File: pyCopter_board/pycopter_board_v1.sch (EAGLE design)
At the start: 53 parts, among them IC1 STM32F405RGT, Q1 8MHz, Q2 32.768kHz, U1 MCP1802

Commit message: Added BNO055 chip library. Also started pyCopter board V1 in board folder. BNO055 connections are almost finished, just need to finish I2C connections.
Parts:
- removed C10, C16, C17: 1u, rcl:C-EUC0603
- removed C11, C12: 12p, rcl:C-EUC0603
- removed C11B, C12B: 2u2, rcl:C-EUC0603
- removed C13, C6, C8, C9: 100n, rcl:C-EUC0603
- removed C7: 4u7, rcl:C-EUC0603
- removed D1: 1N5819, pyboard:1N5819
- removed IC1: STM32F405RGT, pyboard:STM32F405RGT
- removed JBL, JBR1, JBR2, JBR3, JBR4: 1, pinhead:PINHD-1X1
- removed JBOT: 8, pinhead:PINHD-1X8
- removed JLEFT: 14, pinhead:PINHD-1X14
- removed JPOW: 8, pinhead:PINHD-2X4
- removed JRIGHT: 11, pinhead:PINHD-1X11
- removed Q2: 32.768kHz, pyboard:TXC-CRYSTAL32X15
- removed R10, R11: 1k, rcl:R-EU_R0603
- removed R12, R14, R15: 100k, rcl:R-EU_R0603
- removed R13: 10M, rcl:R-EU_R0603
- removed R16: 0, rcl:R-EU_R0603
- removed R17: 10k, rcl:R-EU_R0603
- removed R18: 0, rcl:R-EU_R0805
- removed R5, R6, R7: 560, rcl:R-EU_R0603
- removed U$1, U$6: LTST-C195KGJRKT, pyboard:LTST-C195KGJRKT
- removed U$2, U$3: KMR4TACTILE, pyboard:KMR4TACTILE
- removed U$4: MOLEX-SD-105027, pyboard:MOLEX-SD-105027
- removed U$7: USB-MICRO-AB, pyboard:USB-MICRO-AB
- added JP1, JP2: (no value), SparkFun-Connectors:M14
- C1: value 12p -> 10uF; device rcl:C-EUC0603 -> SparkFun-Passives:CAP0402-CAP
- C2: value 12p -> 0.1uF; device rcl:C-EUC0603 -> SparkFun-Passives:CAP0402-CAP
- C3: value 100n -> 0.1uF; device rcl:C-EUC0603 -> SparkFun-Passives:CAP0402-CAP
- C4, C5: value 100n -> 22pF; device rcl:C-EUC0603 -> SparkFun-Passives:CAP0402-CAP
- Q1: value 8MHz -> 32.768kHz; device pyboard:TXC-CRYSTAL50X32 -> special:XTAL/S
- R1, R2: value 22 -> 10K; device rcl:R-EU_R0603 -> SparkFun-Passives:RESISTOR0402-RES
- R3: value 10k -> 10K; device rcl:R-EU_R0603 -> SparkFun-Passives:RESISTOR0402-RES
- R4: value 560 -> 10K; device rcl:R-EU_R0603 -> SparkFun-Passives:RESISTOR0402-RES
- U1: value MCP1802 -> BNO055; device pyboard:MCP1802 -> BNO055:BNO055
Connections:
- removed net +3V3: C10.1, C17.1, C3.1, C4.1, C5.1, C6.1, C7.1, C8.1, C9.1, IC1.VBAT, IC1.VDD@19, IC1.VDD@32, IC1.VDD@48, IC1.VDD@64, IC1.VDDA, JBL.1, JLEFT.1, R3.1, U$1.A1, U$1.A2, U$4.VDD, U$6.A1, U$6.A2, U1.VOUT
- removed net BOOT0: IC1.BOOT0, JBOT.1, R15.1
- removed net FS_DM: IC1.PA11, R1.2
- removed net FS_DP: IC1.PA12, R2.2
- removed net FS_VUSB: IC1.PA9, R10.2
- removed net IO_PA0: IC1.PA0, JBR4.1
- removed net IO_PA1: IC1.PA1, JBR3.1
- removed net IO_PA14: IC1.PA14, JLEFT.9
- removed net IO_PA15: IC1.PA15, JLEFT.10
- removed net IO_PA2: IC1.PA2, JBR2.1
- removed net IO_PA3: IC1.PA3, JBR1.1
- removed net IO_PA4: IC1.PA4, JRIGHT.11
- removed net IO_PA5: IC1.PA5, JRIGHT.10
- removed net IO_PA6: IC1.PA6, JRIGHT.9
- removed net IO_PA7: IC1.PA7, JRIGHT.8
- removed net IO_PB0: IC1.PB0, JRIGHT.7
- removed net IO_PB1: IC1.PB1, JRIGHT.6
- removed net IO_PB10: IC1.PB10, JRIGHT.5
- removed net IO_PB11: IC1.PB11, JRIGHT.4, R12.1
- removed net IO_PB12: IC1.PB12, JRIGHT.3
- removed net IO_PB13: IC1.PB13, JLEFT.3
- removed net IO_PB14: IC1.PB14, JLEFT.4
- removed net IO_PB15: IC1.PB15, JLEFT.5
- removed net IO_PB2: IC1.PB2, R11.1
- removed net IO_PB3: IC1.PB3, JLEFT.11
- removed net IO_PB4: IC1.PB4, JLEFT.12
- removed net IO_PB9: IC1.PB9, JBOT.4
- removed net IO_PC0: IC1.PC0, JBOT.5
- removed net IO_PC1: IC1.PC1, JBOT.6
- removed net IO_PC2: IC1.PC2, JBOT.7
- removed net IO_PC3: IC1.PC3, JBOT.8
- removed net IO_PC6: IC1.PC6, JLEFT.6
- removed net IO_PC7: IC1.PC7, JLEFT.7
- removed net LEDG1: IC1.PC4, R4.1
- removed net LEDG2: IC1.PC5, R7.1
- removed net LEDR1: IC1.PA8, R6.1
- removed net LEDR2: IC1.PA10, R16.2, R5.1
- removed net MMA_AVDD: IC1.PB5, R14.1
- removed net MMA_INT: IC1.PB8, JBOT.3
- removed net MMA_SCL: IC1.PB6, JLEFT.13
- removed net MMA_SDA: IC1.PB7, JLEFT.14
- removed net N$10: C2.2, IC1.PH0, Q1.P$1
- removed net N$11: R4.2, U$1.K1
- removed net N$12: R5.2, U$6.K2
- removed net N$13: R6.2, U$1.K2
- removed net N$14: R7.2, U$6.K1
- removed net N$15: R17.2, U$3.1@A, U$3.1@B
- removed net N$6: C11.2, IC1.PC15, Q2.P$2
- removed net N$7: R16.1, U$7.ID
- removed net N$9: C1.2, IC1.PH1, Q1.P$2
- removed net NRST: C13.1, IC1.NRST, JBOT.2, R3.2, U$2.1@A, U$2.1@B
- removed net SDIO_CK: IC1.PC12, U$4.CLK
- removed net SDIO_CMD: IC1.PD2, U$4.CMD
- removed net SDIO_D0: IC1.PC8, U$4.DAT0
- removed net SDIO_D1: IC1.PC9, U$4.DAT1
- removed net SDIO_D2: IC1.PC10, U$4.DAT2
- removed net SDIO_D3: IC1.PC11, R13.1, U$4.DAT3
- removed net SDIO_SW: IC1.PC13, U$4.SWITCH
- removed net USR_SW: IC1.PA13, JLEFT.8, R17.1
- removed net VUSB: D1.A, R10.1, R18.2, U$7.VUSB
- new net 3.3V: C1.2, C2.2, JP2.3, R4.1, U1.NBOOT_LOAD_PIN, U1.VDD, U1.VDDIO
- new net LOPY_RST: JP1.14
- new net SCL: U1.COM1
- new net SDA: U1.COM0
- new net XIN: C4.2, Q1.1, U1.XIN32
- new net XOUT: C5.2, Q1.2, U1.XOUT32
- net GND: now also C3.1, C4.1, C5.1, JP2.2, R1.1, R2.1, R3.1, U1.COM2, U1.GNDIO, U1.PIN10, U1.PIN15, U1.PIN16; no longer C10.2, C11.1, C11B.2, C12.1, C12B.2, C13.2, C16.2, C17.2, C3.2, C4.2, C5.2, C6.2, C7.2, C8.2, C9.2, IC1.VSS@18, IC1.VSS@63, IC1.VSSA, JLEFT.2, JPOW.1, JPOW.3, JPOW.5, JPOW.7, JRIGHT.2, R11.2, R12.2, R13.2, R14.2, R15.2, U$2.0@A, U$2.0@B, U$3.0@A, U$3.0@B, U$4.VSS, U$7.GND
- net N$1: now also C3.2, U1.CAP; no longer C11B.1, IC1.VCAP_2
- net N$2: now also R3.2, U1.COM3; no longer C12B.1, IC1.VCAP_1
- net N$3: now also R1.2, U1.PS0; no longer R2.1, U$7.D+
- net N$4: now also R2.2, U1.PS1; no longer R1.1, U$7.D-
- net N$5: now also R4.2, U1.NRESET; no longer C12.2, IC1.PC14, Q2.P$1
- net VIN: now also JP2.1; no longer C16.1, D1.K, JPOW.2, JPOW.4, JPOW.6, JPOW.8, JRIGHT.1, R18.1, U1.EN, U1.VIN
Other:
- note added: "LoPy Headers, 0.1""
- note added: "Need to add I2C circuits"
- note removed: "Analog"
- note removed: "DFU boot"
- note removed: "Deleted Accelerometer Circuit here"
- note removed: "R16 and R18 are unpopulated. Used for optional USB OTG support."
- note removed: "The wires going to the accelerometer were labeled "MMA""
- note removed: "VBAT"
- note removed: "VDD"
- moved on the sheet: C1, C2, C3, C4, C5

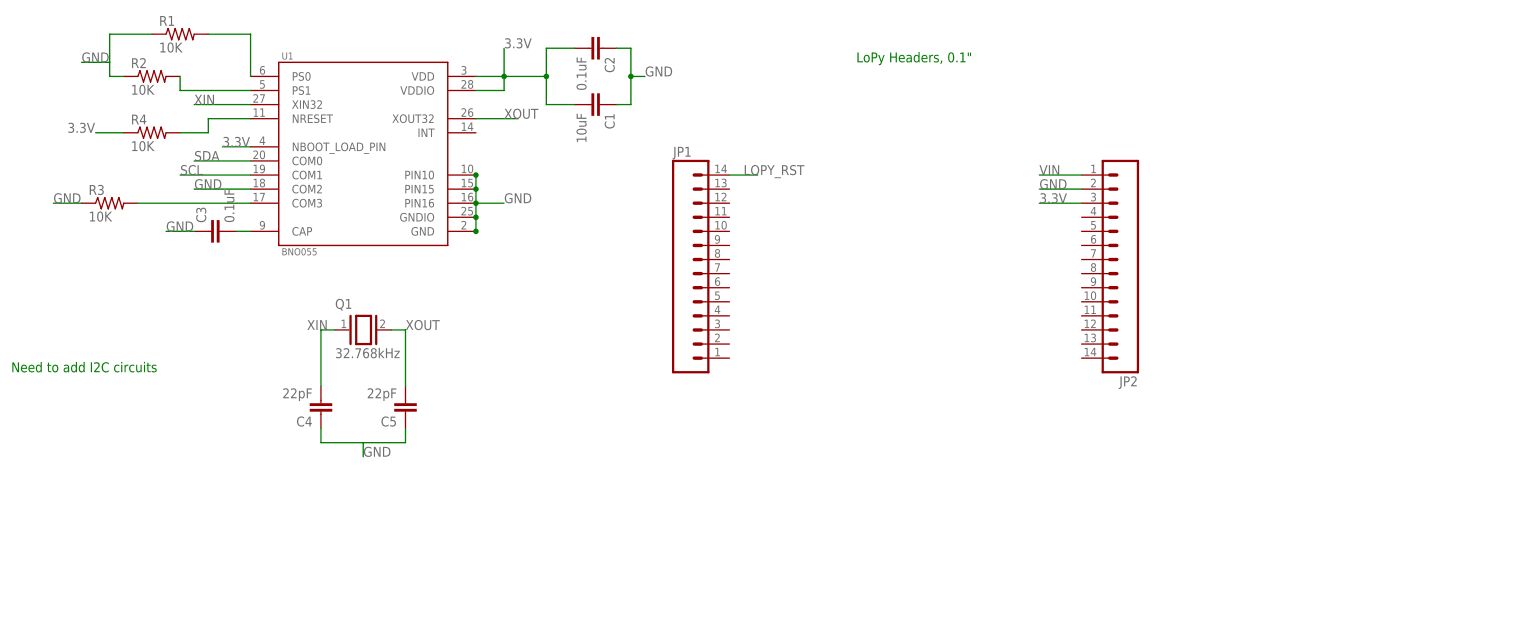
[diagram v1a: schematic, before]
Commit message: Added BMP180 circuit and I2C circuit to schematic. LoPy connections are not complete yet
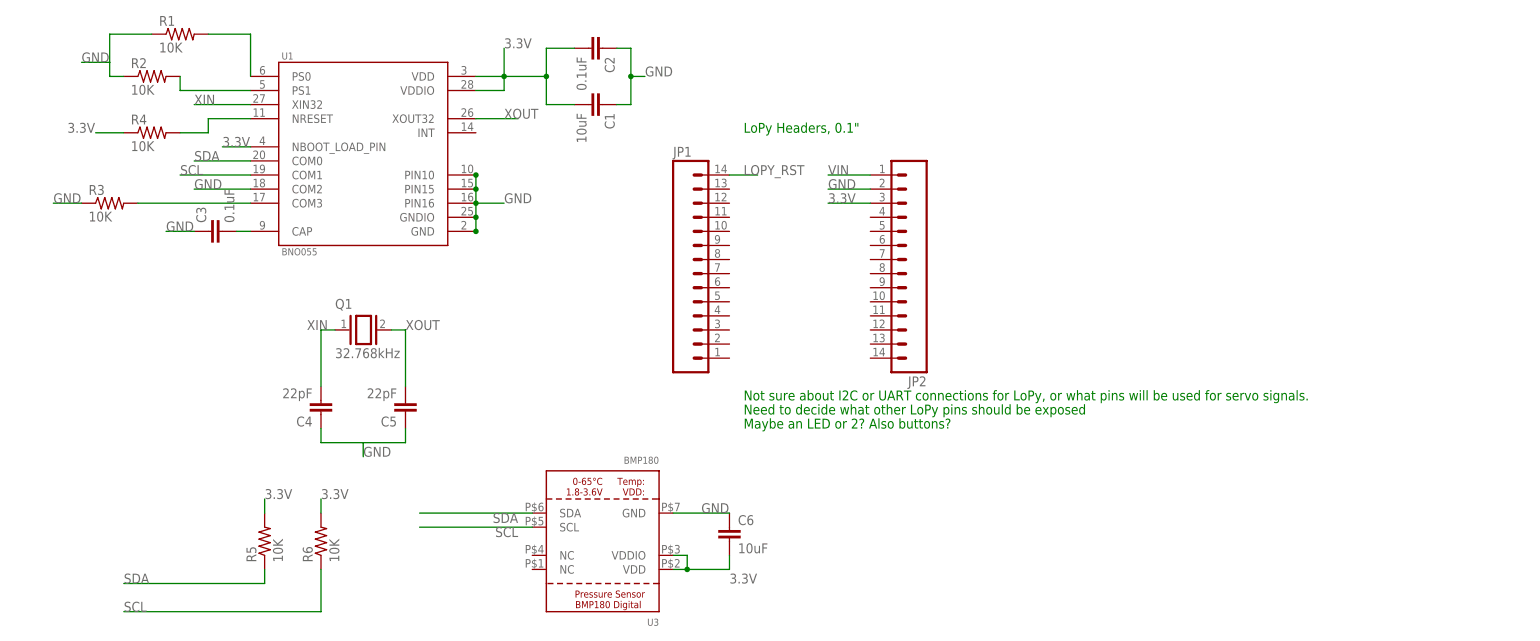
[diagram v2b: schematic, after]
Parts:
- added C6: 10uF, SparkFun-Passives:CAP0402-CAP
- added R5, R6: 10K, SparkFun-Passives:RESISTOR0402-RES
- added U3: BMP180, microbuilder:BMP180EXT
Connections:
- net 3.3V: now also C6.2, R5.2, R6.2, U3.VDD, U3.VDDIO
- net GND: now also C6.1, U3.GND
- net SCL: now also R6.1, U3.SCL
- net SDA: now also R5.1, U3.SDA
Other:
- note added: "Maybe an LED or 2? Also buttons?"
- note added: "Need to decide what other LoPy pins should be exposed"
- note added: "Not sure about I2C or UART connections for LoPy, or what pins will be used for servo signals."
- note removed: "Need to add I2C circuits"
- moved on the sheet: JP2
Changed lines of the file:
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@@
 <part name="R3" library="SparkFun-Passives" deviceset="RESISTOR" device="0402-RES" value="10K"/>
 <part name="R4" library="SparkFun-Passives" deviceset="RESISTOR" device="0402-RES" value="10K"/>
+<part name="R5" library="SparkFun-Passives" deviceset="RESISTOR" device="0402-RES" value="10K"/>
+<part name="R6" library="SparkFun-Passives" deviceset="RESISTOR" device="0402-RES" value="10K"/>
+<part name="U3" library="microbuilder" deviceset="BMP180" device="EXT" value="BMP180"/>
+<part name="C6" library="SparkFun-Passives" deviceset="CAP" device="0402-CAP" value="10uF"/>
 </parts>
 <sheets>
 <sheet>
 <plain>
-<text x="83.82" y="83.82" size="1.778" layer="91">LoPy Headers, 0.1"</text>
-<text x="-68.58" y="27.94" size="1.778" layer="91">Need to add I2C circuits</text>
+<text x="63.5" y="71.12" size="1.778" layer="91">LoPy Headers, 0.1"</text>
+<text x="63.5" y="22.86" size="1.778" layer="91">Not sure about I2C or UART connections for LoPy, or what pins will be used for servo signals.  </text>
+<text x="63.5" y="20.32" size="1.778" layer="91">Need to decide what other LoPy pins should be exposed </text>
+<text x="63.5" y="17.78" size="1.778" layer="91">Maybe an LED or 2? Also buttons?</text>
 </plain>
 <instances>
 <instance part="U1" gate="G$1" x="-5.08" y="68.58"/>
 <instance part="JP1" gate="G$1" x="50.8" y="48.26"/>
-<instance part="JP2" gate="G$1" x="134.62" y="45.72" rot="R180"/>
+<instance part="JP2" gate="G$1" x="96.52" y="45.72" rot="R180"/>
 <instance part="C1" gate="G$1" x="35.56" y="76.2" rot="R270"/>
 <instance part="C2" gate="G$1" x="35.56" y="86.36" rot="R270"/>
@@
 <instance part="R3" gate="G$1" x="-50.8" y="58.42"/>
 <instance part="R4" gate="G$1" x="-43.18" y="71.12"/>
+<instance part="R5" gate="G$1" x="-22.86" y="-2.54" rot="R90"/>
+<instance part="R6" gate="G$1" x="-12.7" y="-2.54" rot="R90"/>
+<instance part="U3" gate="G$1" x="38.1" y="-2.54" rot="R180"/>
+<instance part="C6" gate="G$1" x="60.96" y="-2.54"/>
 </instances>
 <busses>
@@
 <segment>
 <pinref part="JP2" gate="G$1" pin="1"/>
-<wire x1="124.46" y1="63.5" x2="116.84" y2="63.5" width="0.1524" layer="91"/>
-<label x="116.84" y="63.5" size="1.778" layer="95"/>
+<wire x1="86.36" y1="63.5" x2="78.74" y2="63.5" width="0.1524" layer="91"/>
+<label x="78.74" y="63.5" size="1.778" layer="95"/>
 </segment>
 </net>
@@
 <segment>
 <pinref part="JP2" gate="G$1" pin="2"/>
-<wire x1="124.46" y1="60.96" x2="116.84" y2="60.96" width="0.1524" layer="91"/>
-<label x="116.84" y="60.96" size="1.778" layer="95"/>
+<wire x1="86.36" y1="60.96" x2="78.74" y2="60.96" width="0.1524" layer="91"/>
+<label x="78.74" y="60.96" size="1.778" layer="95"/>
 </segment>
 <segment>
@@
 <label x="-60.96" y="58.42" size="1.778" layer="95"/>
 </segment>
+<segment>
+<pinref part="U3" gate="G$1" pin="GND"/>
+<wire x1="50.8" y1="2.54" x2="60.96" y2="2.54" width="0.1524" layer="91"/>
+<label x="55.88" y="2.54" size="1.778" layer="95"/>
+<pinref part="C6" gate="G$1" pin="1"/>
+</segment>
 </net>
 <net name="3.3V" class="0">
 <segment>
 <pinref part="JP2" gate="G$1" pin="3"/>
-<wire x1="124.46" y1="58.42" x2="116.84" y2="58.42" width="0.1524" layer="91"/>
-<label x="116.84" y="58.42" size="1.778" layer="95"/>
+<wire x1="86.36" y1="58.42" x2="78.74" y2="58.42" width="0.1524" layer="91"/>
+<label x="78.74" y="58.42" size="1.778" layer="95"/>
 </segment>
 <segment>
@@
 <label x="-58.42" y="71.12" size="1.778" layer="95"/>
 </segment>
+<segment>
+<pinref part="R5" gate="G$1" pin="2"/>
+<wire x1="-22.86" y1="2.54" x2="-22.86" y2="5.08" width="0.1524" layer="91"/>
+<label x="-22.86" y="5.08" size="1.778" layer="95"/>
+</segment>
+<segment>
+<pinref part="R6" gate="G$1" pin="2"/>
+<wire x1="-12.7" y1="2.54" x2="-12.7" y2="5.08" width="0.1524" layer="91"/>
+<label x="-12.7" y="5.08" size="1.778" layer="95"/>
+</segment>
+<segment>
+<pinref part="U3" gate="G$1" pin="VDDIO"/>
+<wire x1="50.8" y1="-5.08" x2="53.34" y2="-5.08" width="0.1524" layer="91"/>
+<wire x1="53.34" y1="-5.08" x2="53.34" y2="-7.62" width="0.1524" layer="91"/>
+<pinref part="U3" gate="G$1" pin="VDD"/>
+<wire x1="50.8" y1="-7.62" x2="53.34" y2="-7.62" width="0.1524" layer="91"/>
+<junction x="53.34" y="-7.62"/>
+<pinref part="C6" gate="G$1" pin="2"/>
+<wire x1="53.34" y1="-7.62" x2="60.96" y2="-7.62" width="0.1524" layer="91"/>
+<wire x1="60.96" y1="-7.62" x2="60.96" y2="-5.08" width="0.1524" layer="91"/>
+<label x="60.96" y="-10.16" size="1.778" layer="95"/>
+</segment>
 </net>
 <net name="LOPY_RST" class="0">
@@
 <label x="-35.56" y="66.04" size="1.778" layer="95"/>
 </segment>
+<segment>
+<wire x1="-48.26" y1="-10.16" x2="-22.86" y2="-10.16" width="0.1524" layer="91"/>
+<wire x1="-22.86" y1="-10.16" x2="-22.86" y2="-7.62" width="0.1524" layer="91"/>
+<pinref part="R5" gate="G$1" pin="1"/>
+<label x="-48.26" y="-10.16" size="1.778" layer="95"/>
+</segment>
+<segment>
+<wire x1="25.4" y1="2.54" x2="5.08" y2="2.54" width="0.1524" layer="91"/>
+<label x="22.86" y="2.54" size="1.778" layer="95" rot="R180"/>
+<pinref part="U3" gate="G$1" pin="SDA"/>
+</segment>
 </net>
 <net name="SCL" class="0">
@@
 <label x="-38.1" y="63.5" size="1.778" layer="95"/>
 </segment>
-</net>
+<segment>
+<wire x1="-48.26" y1="-15.24" x2="-12.7" y2="-15.24" width="0.1524" layer="91"/>
+<wire x1="-12.7" y1="-15.24" x2="-12.7" y2="-7.62" width="0.1524" layer="91"/>
+<pinref part="R6" gate="G$1" pin="1"/>
+<label x="-48.26" y="-15.24" size="1.778" layer="95"/>
+</segment>
+<segment>
+<wire x1="5.08" y1="0" x2="25.4" y2="0" width="0.1524" layer="91"/>
+<label x="22.86" y="0" size="1.778" layer="95" rot="R180"/>
+<pinref part="U3" gate="G$1" pin="SCL"/>
+</segment>
+</net>
